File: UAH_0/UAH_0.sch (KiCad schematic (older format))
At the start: 60 parts, among them X1 Check_point, X2 Check_point, X3 Крепежное_отверстие_М3, X4 Крепежное_отверстие_М3, X5 Крепежное_отверстие_М3, X6 Крепежное_отверстие_М3, X7 LOGO_NIKITOS_19х7

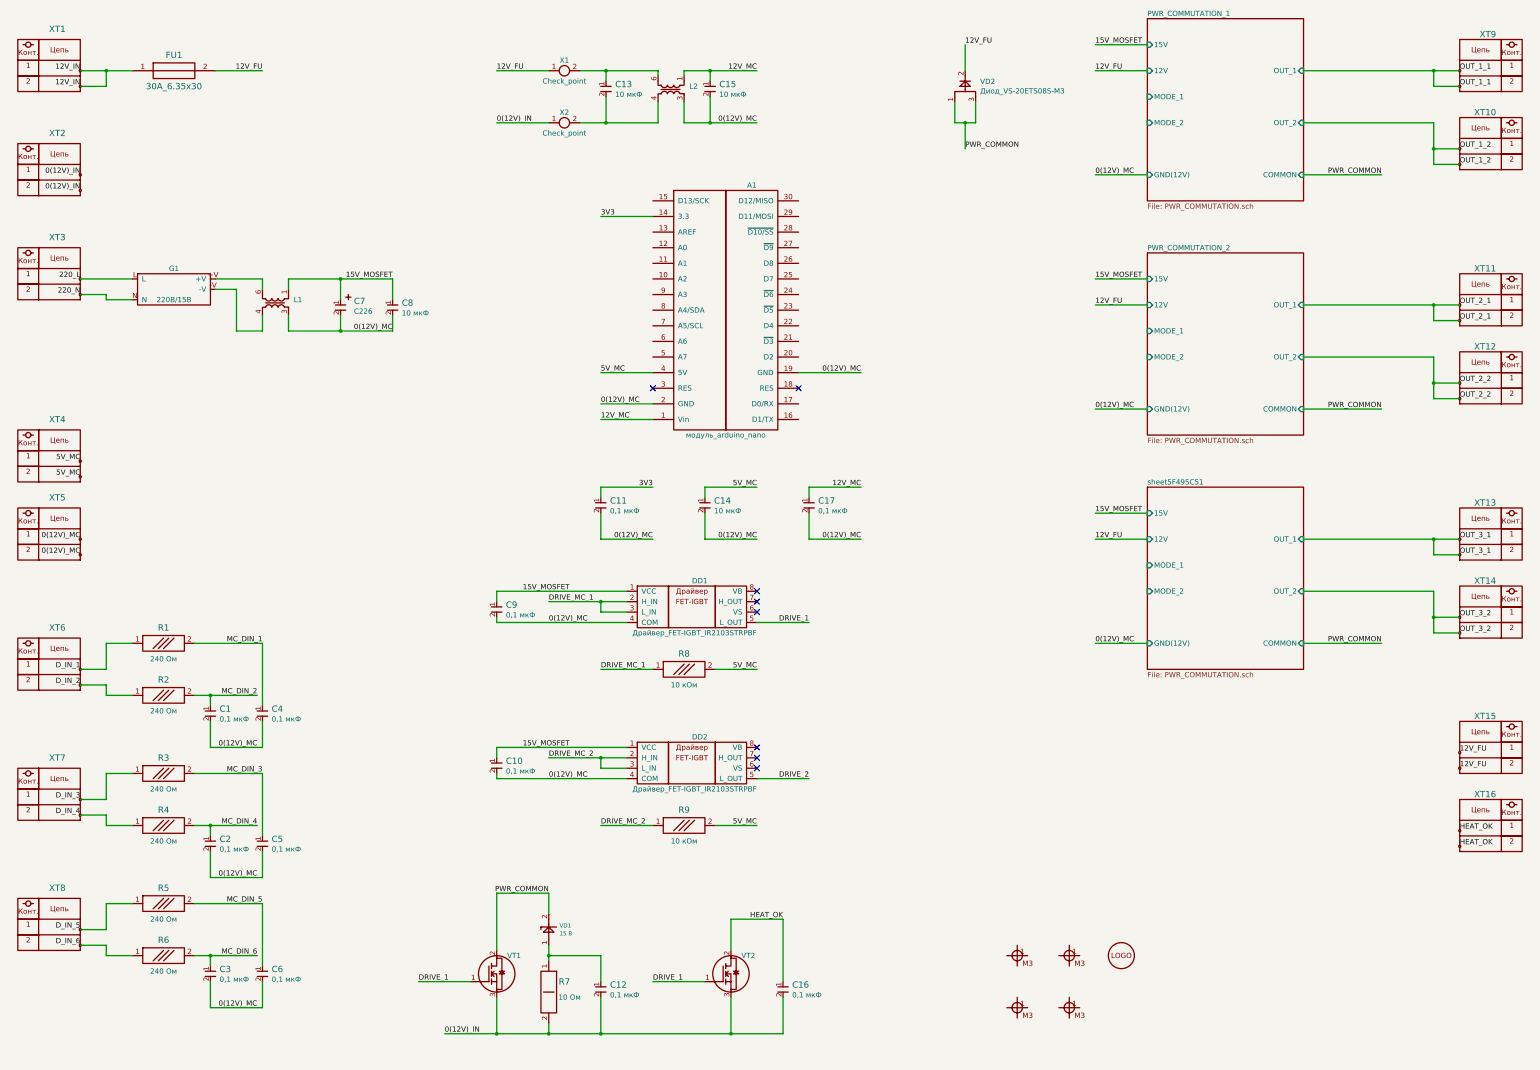
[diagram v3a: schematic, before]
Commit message: не подведены управления DI, габарит определен
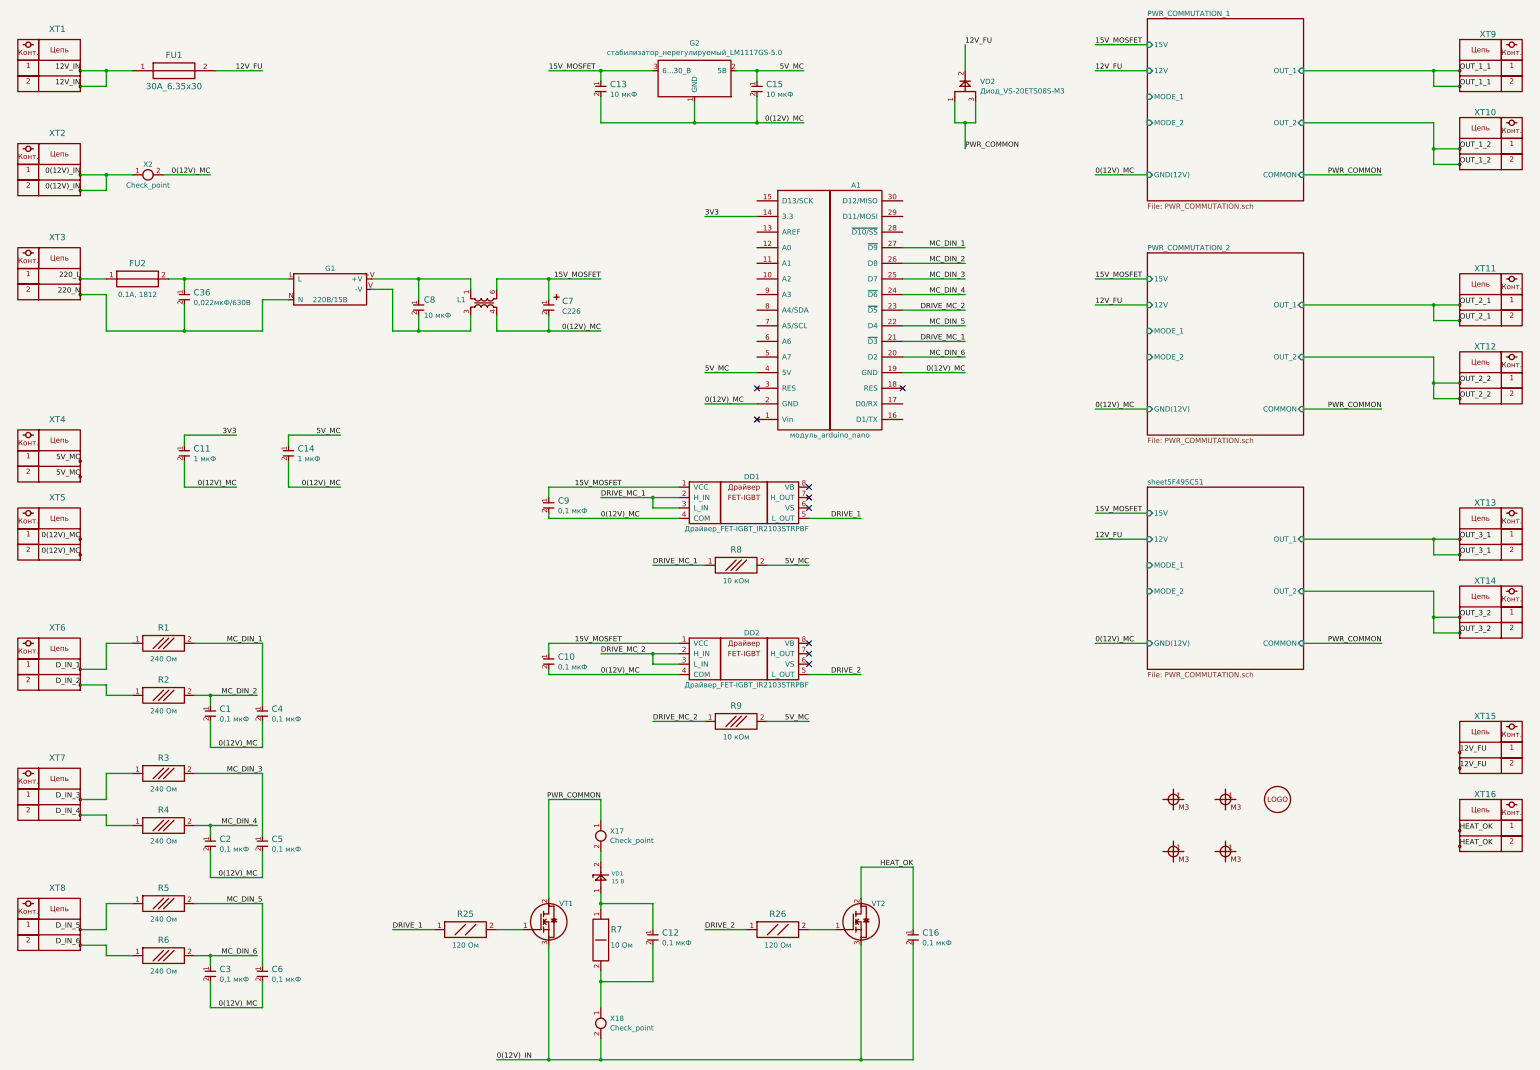
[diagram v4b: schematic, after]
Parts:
- removed C17: Конденсатор_16В_0.1_мкФ+-10проц., MOTOR_RLC:Конденсатор_SMD_К10-83(0603), symbol MOTOR_2020_import:Конденсатор_16В_0.1_мкФ+-10проц.
- removed L2: Дроссель_B82731-T2451-A20_2х47мГн_0.45А_250В, N_RLC:Дроссель_B82731, symbol elements_2020:Дроссель_B82731-T2451-A20_2х47мГн_0.45А_250В
- removed X1: Check_point, N_X:Пробник, symbol elements_2020:Check_point
- added C36: Конденсатор_0.022мкФ_10проц_630В_1210, MOTOR_RLC:Конденсатор_SMD_1210, symbol MOTOR_2020_components:Конденсатор_К10-83-25В-0,1_мкФ+-20проц.
- added FU2: Предохранитель_MF-MSMF010_0,1А_1812, N_RLC:Предохранитель_SMD_1812, symbol elements_2020:Предохранитель_MF-MSMF160_1,6А_1812
- added G2: стабилизатор_нерегулируемый_LM1117GS-5.0, N_VD_HL:Транзистор_NPN_SOT223, symbol elements:стабилизатор_нерегулируемый_LM1117GS-5.0
- added R25, R26: Резистор_Р1-12-0,125-120_Ом±5%-Н-«А», MOTOR_RLC:Резистор_SMD_0805_0,125Вт, symbol MOTOR_2020_components:Резистор_Р1-12-0,125-120_Ом±5%-Н-«А»
- added X17, X18: Check_point, N_X:Пробник, symbol elements_2020:Check_point
- C11: INFO 0,1 мкФ -> 1 мкФ
- C14: footprint MOTOR_RLC:Конденсатор_SMD_0805 -> MOTOR_RLC:Конденсатор_SMD_К10-83(0603); INFO 10 мкФ -> 1 мкФ
- XT4, XT5, XT6, XT7, XT8: footprint N_X:Клеммник_х2_шаг5 -> N_X:Клеммник_х2_шаг2.54
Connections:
- net 0(12V)_IN: now also X18.2; no longer C12.2, R7.2
- net 0(12V)_MC: now also C13.2, L1.4, X2.2, G2.1 (GND); no longer C8.2, L1.3
- net 15V_MOSFET: now also C13.1, L1.6, G2.3 (6...30_В); no longer C8.1, L1.1
- net 220_L: now also FU2.1; no longer G1.L
- net 220_N: now also C36.2
- net 5V_MC: now also C15.1, G2.2 (5В)
- net DRIVE_1: now also R25.1; no longer VT1.1, VT2.1
- net DRIVE_2: now also R26.1
- net DRIVE_MC_1: now also A1.21 (~D3)
- net DRIVE_MC_2: now also A1.23 (~D5)
- net MC_DIN_1: now also A1.27 (~D9)
- net MC_DIN_2: now also A1.26 (D8)
- net MC_DIN_3: now also A1.25 (D7)
- net MC_DIN_4: now also A1.24 (~D6)
- net MC_DIN_5: now also A1.22 (D4)
- net MC_DIN_6: now also A1.20 (D2)
- net PWR_COMMON: now also X17.1; no longer VD1.2
- net at G1.-V: now also C8.2, L1.3; no longer L1.4
- net at G1.+V: now also C8.1, L1.1; no longer L1.6
- net 12V_MC: no longer names the net of A1.1 (Vin)
- net 12V_MC: no longer C15.1
- new net: R25.2, VT1.1
- new net: C12.2, R7.2, X18.1
- new net: VD1.2, X17.2
- new net: C36.1, FU2.2, G1.L
- new net: R26.2, VT2.1
- no-connect marks 8 -> 9
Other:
- moved on the sheet: A1, C10, C11, C12, C13, C14, C15, C16, C7, C8, C9, DD1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
